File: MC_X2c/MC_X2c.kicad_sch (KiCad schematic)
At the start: 0 parts

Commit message: Working progress - migration to MAC
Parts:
- added C34: 100nF, symbol Device:C
- added J13: ESP Flash Port, Connector_Harwin:Harwin_M20-89006xx_1x06_P2.54mm_Horizontal, symbol Connector:Conn_01x06_Pin
- added MCP0, MCP1, MCP2: MCP23017_ML, Package_DFN_QFN:QFN-28-1EP_6x6mm_P0.65mm_EP4.25x4.25mm, symbol Interface_Expansion:MCP23017_ML
- added R1, R102, R103, R104, R105, R106, R107, R108, R109, R110, R111, R112, R113, R114, R115, R116, R117, R118, R119, R4, R5: 10k, symbol Device:R
- added R2, R3: 4.7k, symbol Device:R
- added U1: ESP32-C6-MINI-1, RF_Module:ESP32-C6-MINI-1, symbol RF_Module:ESP32-C6-MINI-1
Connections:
- new net: MCP2.24 (GPA7), R109.2
- new net: MCP1.12 (A1), R4.1
- new net: J13.5 (Pin_5), U1.12 (IO0)
- new net: J13.1 (Pin_1), U1.30 (RXD0)
- new net: J13.2 (Pin_2), U1.31 (TXD0)
- new net: C34.2, J13.4 (Pin_4), R103.1, U1.8 (EN)
- new net: MCP1.24 (GPA7), R107.2
- new net: MCP2.18 (GPA1), R115.2
- new net: MCP1.16 (INTA), R119.1
- new net: MCP1.21 (GPA4), R108.2
- new net: MCP1.22 (GPA5), R106.2
- new net: MCP1.23 (GPA6), R105.2
- new net: MCP0.16 (INTA), R118.1
- new net: MCP2.21 (GPA4), R112.2
- new net: MCP2.16 (INTA), R117.1
- new net: MCP0.11 (A0), R1.1
- new net: MCP2.20 (GPA3), R113.2
- new net: MCP2.13 (A2), R5.1
- new net: MCP2.19 (GPA2), R114.2
- new net: MCP2.23 (GPA6), R110.2
- new net: MCP2.22 (GPA5), R111.2
- new net: MCP2.17 (GPA0), R116.2
- new net +3V3: J13.3 (Pin_3), MCP0.5 (VDD), MCP1.5 (VDD), MCP2.5 (VDD), R1.2, R102.2, R103.2, R104.1, R117.2, R118.2, R119.2, R2.2, R3.1, R4.2, R5.2, U1.3 (3V3)
- new net C10_RA_MCP2: MCP2.27 (GPB2)
- new net C10_RC_MCP1: MCP1.18 (GPA1)
- new net C10_SP_MCP2: MCP2.28 (GPB3)
- new net C1C_RA_MCP2: MCP2.1 (GPB4)
- new net C1C_RC_MCP1: MCP1.19 (GPA2)
- new net C1C_SP_MCP2: MCP2.2 (GPB5)
- new net C1_RA_MCP0: MCP0.26 (GPB1)
- new net C1_RC_MCP0: MCP0.17 (GPA0)
- new net C1_SP_MCP0: MCP0.25 (GPB0)
- new net C2C_RA_MCP2: MCP2.3 (GPB6)
- new net C2C_RC_MCP1: MCP1.20 (GPA3)
- new net C2C_SP_MCP2: MCP2.4 (GPB7)
- new net C2_RA_MCP0: MCP0.28 (GPB3)
- new net C2_RC_MCP0: MCP0.18 (GPA1)
- new net C2_SP_MCP0: MCP0.27 (GPB2)
- new net C3_RA_MCP0: MCP0.2 (GPB5)
- new net C3_RC_MCP0: MCP0.19 (GPA2)
- new net C3_SP_MCP0: MCP0.1 (GPB4)
- new net C4_RA_MCP0: MCP0.4 (GPB7)
- new net C4_RC_MCP0: MCP0.20 (GPA3)
- new net C4_SP_MCP0: MCP0.3 (GPB6)
- new net C5_RA_MCP1: MCP1.25 (GPB0)
- new net C5_RC_MCP0: MCP0.21 (GPA4)
- new net C5_SP_MCP1: MCP1.26 (GPB1)
- new net C6_RA_MCP1: MCP1.27 (GPB2)
- new net C6_RC_MCP0: MCP0.22 (GPA5)
- new net C6_SP_MCP1: MCP1.28 (GPB3)
- new net C7_RA_MCP1: MCP1.1 (GPB4)
- new net C7_RC_MCP0: MCP0.23 (GPA6)
- new net C7_SP_MCP1: MCP1.2 (GPB5)
- new net C8_RA_MCP1: MCP1.3 (GPB6)
- new net C8_RC_MCP0: MCP0.24 (GPA7)
- new net C8_SP_MCP1: MCP1.4 (GPB7)
- new net C9_RA_MCP2: MCP2.25 (GPB0)
- new net C9_RC_MCP1: MCP1.17 (GPA0)
- new net C9_SP_MCP2: MCP2.26 (GPB1)
- new net GND: C34.1, J13.6 (Pin_6), MCP0.12 (A1), MCP0.13 (A2), MCP0.29 (EP), MCP0.6 (VSS), MCP1.11 (A0), MCP1.13 (A2), MCP1.29 (EP), MCP1.6 (VSS), MCP2.11 (A0), MCP2.12 (A1), MCP2.29 (EP), MCP2.6 (VSS), R105.1, R106.1, R107.1, R108.1, R109.1, R110.1, R111.1, R112.1, R113.1, R114.1, R115.1, R116.1, U1.1 (GND), U1.11 (GND), U1.14 (GND), U1.2 (GND), U1.36 (GND), U1.37 (GND), U1.38 (GND), U1.39 (GND), U1.40 (GND), U1.41 (GND), U1.42 (GND), U1.43 (GND), U1.44 (GND), U1.45 (GND), U1.46 (GND), U1.47 (GND), U1.48 (GND), U1.49 (GND), U1.50 (GND), U1.51 (GND), U1.52 (GND), U1.53 (GND)
- new net I2C_SCK: MCP0.8 (SCK), MCP1.8 (SCK), MCP2.8 (SCK), R3.2, U1.28 (IO22)
- new net I2C_SDA: MCP0.9 (SDA), MCP1.9 (SDA), MCP2.9 (SDA), R2.1, U1.27 (IO21)
- new net INT_MCP: MCP0.15 (INTB), MCP1.15 (INTB), MCP2.15 (INTB), R104.2, U1.9 (IO4)
- new net MCP_RESET: MCP0.14 (~{RESET}), MCP1.14 (~{RESET}), MCP2.14 (~{RESET}), R102.1, U1.25 (IO19)
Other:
- sheet channel renamed channel1
- added sheet channel10 (channel.kicad_sch)
- added sheet channel1c (channel.kicad_sch)
- added sheet channel2 (channel.kicad_sch)
- added sheet channel2c (channel.kicad_sch)
- added sheet channel3 (channel.kicad_sch)
- added sheet channel4 (channel.kicad_sch)
- added sheet channel5 (channel.kicad_sch)
- added sheet channel6 (channel.kicad_sch)
- added sheet channel7 (channel.kicad_sch)
- added sheet channel8 (channel.kicad_sch)
- added sheet channel9 (channel.kicad_sch)
- sheet ac_entry ports: added 3V3, 5V0, AC_N, AC_PE, GND, ­AC_L; removed none
- sheet channel1 ports: added AC_L, AC_N, F_RA, F_SP, RC; removed none
- company: (none) -> Nelees
- title: (none) -> MC-X2c

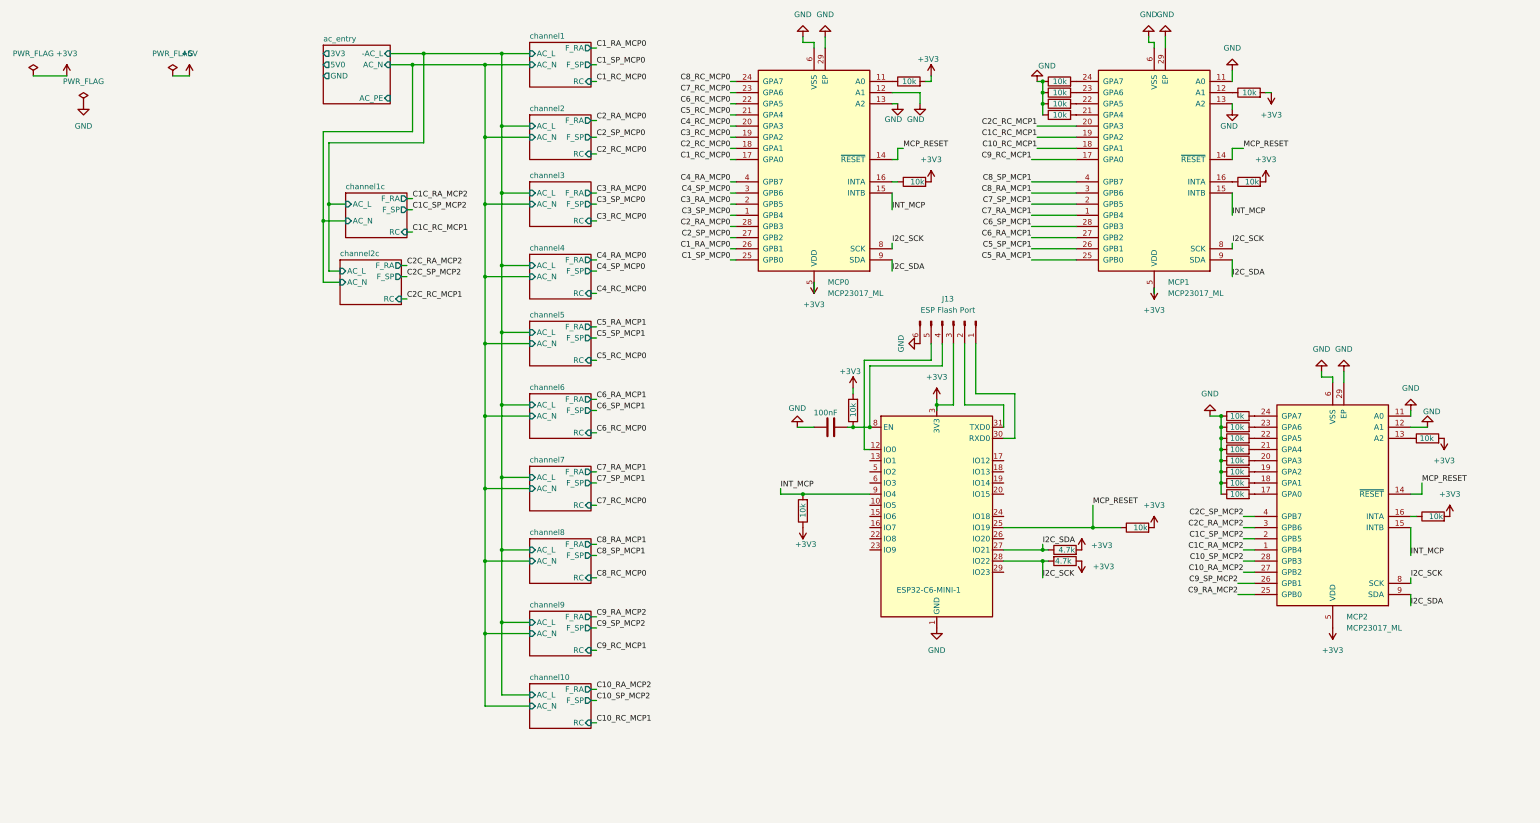
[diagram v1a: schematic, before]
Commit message: Proper namings in AC_ENTRY and CHANNEL + passives on root
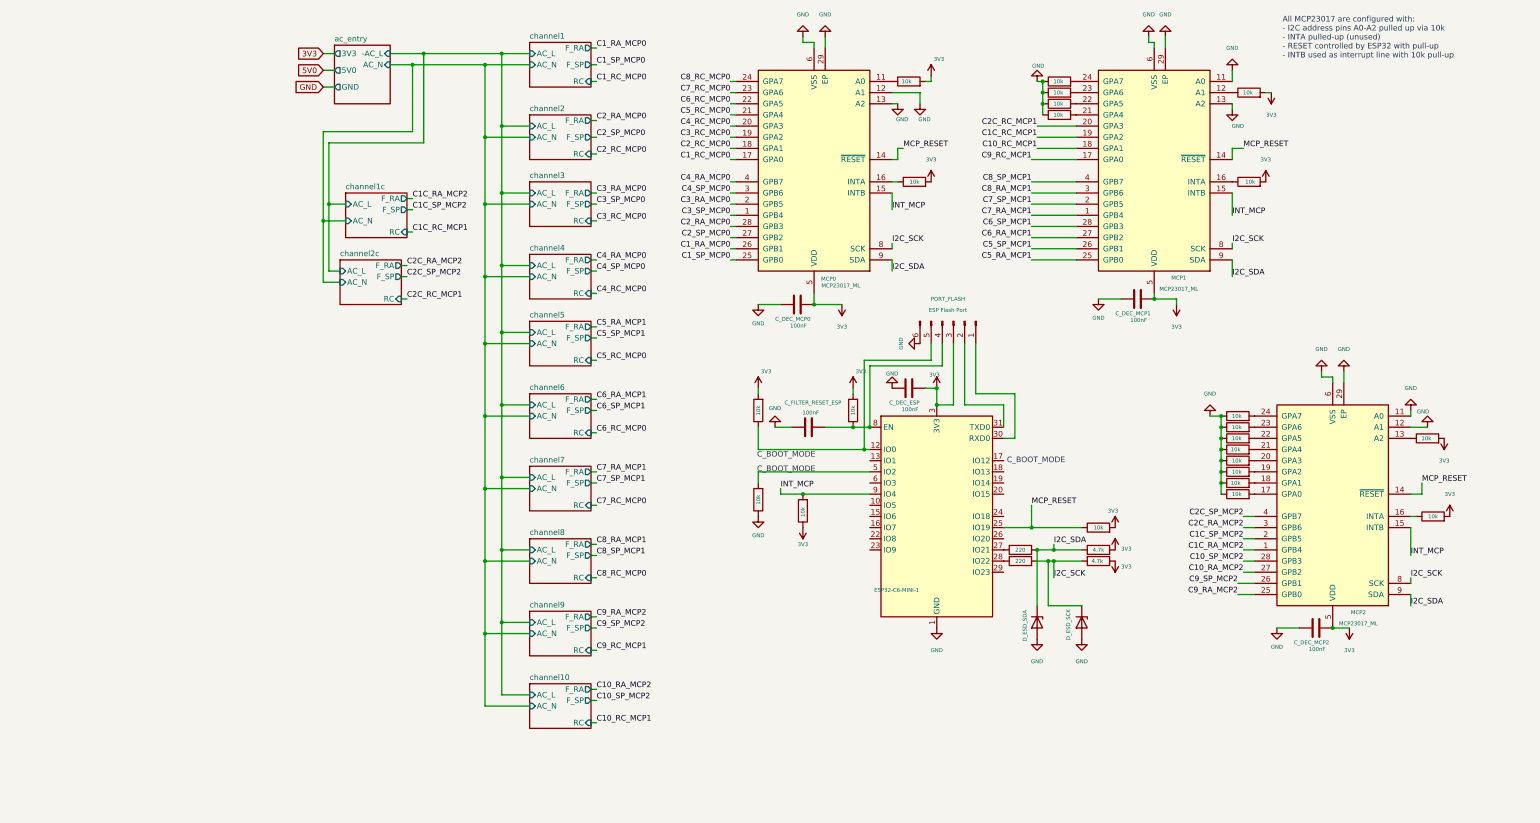
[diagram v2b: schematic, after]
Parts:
- added C_DEC_ESP, C_DEC_MCP0, C_DEC_MCP1, C_DEC_MCP2: 100nF, symbol Device:C
- added D_ESD_SCK, D_ESD_SDA: ESD5Z3.3, Diode_SMD:D_SOD-523, symbol Diode:ESD5Zxx
- added R_PULLUP_RESET_ESP1, R_PULLUP_RESET_ESP2: 10k, symbol Device:R
- added R_SCK_SER1, R_SDA_SER: 220, symbol Device:R
- renumbered C34 to C_FILTER_RESET_ESP, U1 to MAIN_MCU, J13 to PORT_FLASH, R107 to R_PULLDOWN1, R114 to R_PULLDOWN10, R115 to R_PULLDOWN11, R116 to R_PULLDOWN12, R105 to R_PULLDOWN2, R106 to R_PULLDOWN3, R108 to R_PULLDOWN4, R109 to R_PULLDOWN5, R110 to R_PULLDOWN6, R111 to R_PULLDOWN7, R112 to R_PULLDOWN8, R113 to R_PULLDOWN9, R118 to R_PULLUP_INTA0, R104 to R_PULLUP_INTB, R103 to R_PULLUP_RESET_ESP, R102 to R_PULLUP_RESET_MCP, R3 to R_PULLUP_SCK, R2 to R_PULLUP_SDA, R119 to R_PU_INTA1, R117 to R_PU_INTA2, R1 to R_PU_MCP0_A0, R4 to R_PU_MCP1_A1, R5 to R_PU_MCP2_A2
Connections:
- net GND: now also C_DEC_ESP.1, C_DEC_MCP0.1, C_DEC_MCP1.1, C_DEC_MCP2.1, D_ESD_SCK.2 (A), D_ESD_SDA.2 (A), R_PULLUP_RESET_ESP2.1
- net I2C_SCK: now also D_ESD_SCK.1 (K), R_SCK_SER1.2; no longer MAIN_MCU.28 (IO22)
- net I2C_SDA: now also D_ESD_SDA.1 (K), R_SDA_SER.2; no longer MAIN_MCU.27 (IO21)
- net at MAIN_MCU.12 (IO0), PORT_FLASH.5 (Pin_5): now also R_PULLUP_RESET_ESP1.1
- net at MAIN_MCU.5 (IO2): now also R_PULLUP_RESET_ESP2.2
- net +3V3 renamed 3V3
- net 3V3: now also C_DEC_ESP.2, C_DEC_MCP0.2, C_DEC_MCP1.2, C_DEC_MCP2.2, R_PULLUP_RESET_ESP1.2
- new net: MAIN_MCU.27 (IO21), R_SDA_SER.1
- new net: MAIN_MCU.28 (IO22), R_SCK_SER1.1
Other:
- sheet ac_entry ports: added none; removed AC_PE
- note added: "All MCP23017 are configured with: - I2C address pins A0-A2 pulled up via 10k - INTA pulled-up (unused) - RESET controlled by ESP32 with pull-up - INTB used as interrupt line with 10k pull-up"
- note added: "C_BOOT_MODE"

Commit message: Fix channel refference names and add fuse for channel out
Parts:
- renumbered C_DEC_ESP to C_DEC_ESP1, C_DEC_MCP0 to C_DEC_MCP1, C_DEC_MCP1 to C_DEC_MCP2, C_DEC_MCP2 to C_DEC_MCP3, C_FILTER_RESET_ESP to C_FILTER_RESET_ESP1, D_ESD_SCK to D_ESD_SCK1, D_ESD_SDA to D_ESD_SDA1, MAIN_MCU to MAIN_MCU1, MCP0 to MCP1, MCP1 to MCP2, MCP2 to MCP3, PORT_FLASH to PORT_FLASH1, R_PULLUP_INTA0 to R_PULLUP_INTA1, R_PULLUP_INTB to R_PULLUP_INTB1, R_PULLUP_RESET_ESP to R_PULLUP_RESET_ESP3, R_PULLUP_RESET_MCP to R_PULLUP_RESET_MCP1, R_PULLUP_SCK to R_PULLUP_SCK1, R_PULLUP_SDA to R_PULLUP_SDA1, R_PU_MCP0_A0 to R_PU_MCP0_A1, R_PU_MCP2_A2 to R_PU_MCP2_A1, R_SDA_SER to R_SDA_SER1
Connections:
- no-connect marks 0 -> 14

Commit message: Replace MCU with ESP32-S3 and added SPI and RF433 ports
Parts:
- added C_FILTER_RESET_MCP1: 100nF, symbol Device:C
- added C_FILTER_RF1: 100pF, symbol Device:C
- added PORT_RF433mhz1: SRX882 Port, Connector_JST:JST_EH_B4B-EH-A_1x04_P2.50mm_Vertical, symbol Connector:Conn_01x04_Pin
- added SPI_PORT1: SPI_PORT, symbol Connector:Conn_01x08_Pin
- MAIN_MCU1: value ESP32-C6-MINI-1 -> ESP32-S3-WROOM-1; footprint RF_Module:ESP32-C6-MINI-1 -> RF_Module:ESP32-S3-WROOM-1; symbol RF_Module:ESP32-C6-MINI-1 -> RF_Module:ESP32-S3-WROOM-1
- R_SCK_SER1, R_SDA_SER1: value 220 -> 100
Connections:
- net 3V3: now also MAIN_MCU1.2 (3V3), R_PULLUP_RESET_ESP2.2, R_PULLUP_SCK1.2, R_PULLUP_SDA1.1, PORT_RF433mhz1.1 (Pin_1), SPI_PORT1.1 (Pin_1); no longer MAIN_MCU1.3 (3V3), R_PULLUP_SCK1.1, R_PULLUP_SDA1.2
- net GND: now also C_FILTER_RESET_MCP1.1, C_FILTER_RF1.1, PORT_RF433mhz1.2 (Pin_2), SPI_PORT1.8 (Pin_8); no longer MAIN_MCU1.11 (GND), MAIN_MCU1.14 (GND), MAIN_MCU1.2 (GND), MAIN_MCU1.36 (GND), MAIN_MCU1.37 (GND), MAIN_MCU1.38 (GND), MAIN_MCU1.39 (GND), MAIN_MCU1.42 (GND), MAIN_MCU1.43 (GND), MAIN_MCU1.44 (GND), MAIN_MCU1.45 (GND), MAIN_MCU1.46 (GND), MAIN_MCU1.47 (GND), MAIN_MCU1.48 (GND), MAIN_MCU1.49 (GND), MAIN_MCU1.50 (GND), MAIN_MCU1.51 (GND), MAIN_MCU1.52 (GND), MAIN_MCU1.53 (GND), R_PULLUP_RESET_ESP2.1
- net I2C_SDA: now also R_PULLUP_SDA1.2, R_SDA_SER1.1; no longer R_PULLUP_SDA1.1, R_SDA_SER1.2
- net INT_MCP: now also MAIN_MCU1.4 (IO4); no longer MAIN_MCU1.9 (IO4)
- net MCP_RESET: now also MAIN_MCU1.8 (IO15), C_FILTER_RESET_MCP1.2; no longer MAIN_MCU1.25 (IO19)
- net SPI_CE/RESET: now reaches MAIN_MCU1.10 (IO17)
- net SPI_CE/RESET: now also SPI_PORT1.4 (Pin_4)
- net at PORT_FLASH1.5 (Pin_5), R_PULLUP_RESET_ESP1.1: now also MAIN_MCU1.27 (IO0); no longer MAIN_MCU1.12 (IO0)
- net SPI_DIO0 (IRQ) : now reaches MAIN_MCU1.17 (IO9)
- net SPI_DIO0 (IRQ) : now also SPI_PORT1.2 (Pin_2)
- net SPI_CSN/NSS: now reaches MAIN_MCU1.18 (IO10)
- net SPI_CSN/NSS: now also SPI_PORT1.3 (Pin_3)
- net SPI_MISO: now reaches MAIN_MCU1.20 (IO12)
- net SPI_MISO: now also SPI_PORT1.5 (Pin_5)
- net SPI_MOSI: now reaches MAIN_MCU1.21 (IO13)
- net SPI_MOSI: now also SPI_PORT1.6 (Pin_6)
- net SPI_SCK: now reaches MAIN_MCU1.22 (IO14)
- net SPI_SCK: now also SPI_PORT1.7 (Pin_7)
- net at MAIN_MCU1.28 (IO35): no longer R_SCK_SER1.1
- net at MAIN_MCU1.30 (IO37): no longer PORT_FLASH1.1 (Pin_1)
- net at MAIN_MCU1.31 (IO38): no longer PORT_FLASH1.2 (Pin_2)
- net at MAIN_MCU1.5 (IO5): no longer R_PULLUP_RESET_ESP2.2
- net at MAIN_MCU1.6 (IO6): now also R_SDA_SER1.2
- net at MAIN_MCU1.7 (IO7): now also R_SCK_SER1.2
- net at C_FILTER_RESET_ESP1.2, PORT_FLASH1.4 (Pin_4), R_PULLUP_RESET_ESP3.1: now also MAIN_MCU1.3 (EN); no longer MAIN_MCU1.8 (EN)
- net I2C_SCK renamed I2C_SCL
- net I2C_SCL: now also R_PULLUP_SCK1.1, R_SCK_SER1.1; no longer R_PULLUP_SCK1.2, R_SCK_SER1.2
- new net: C_FILTER_RF1.2, MAIN_MCU1.9 (IO16), PORT_RF433mhz1.3 (Pin_3)
- new net: MAIN_MCU1.36 (RXD0), PORT_FLASH1.1 (Pin_1)
- new net: MAIN_MCU1.37 (TXD0), PORT_FLASH1.2 (Pin_2)
- new net: MAIN_MCU1.38 (IO2), R_PULLUP_RESET_ESP2.1
- no-connect marks 14 -> 22
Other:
- moved on the sheet: C_FILTER_RESET_ESP1, D_ESD_SCK1, D_ESD_SDA1
